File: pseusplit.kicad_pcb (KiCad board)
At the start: 2 copper layers, 231.4 x 82.6 mm, 146 parts, among them J1 USB_C_Receptacle_USB2.0_14P, J3 ST7789 320x240, Q1 DTC123J, SW1 Reset_SW, U1 IS31FL3733-QF, U2 XC6206PxxxMR, U4 STM32G0B1CBTx, U5 SRV05-4

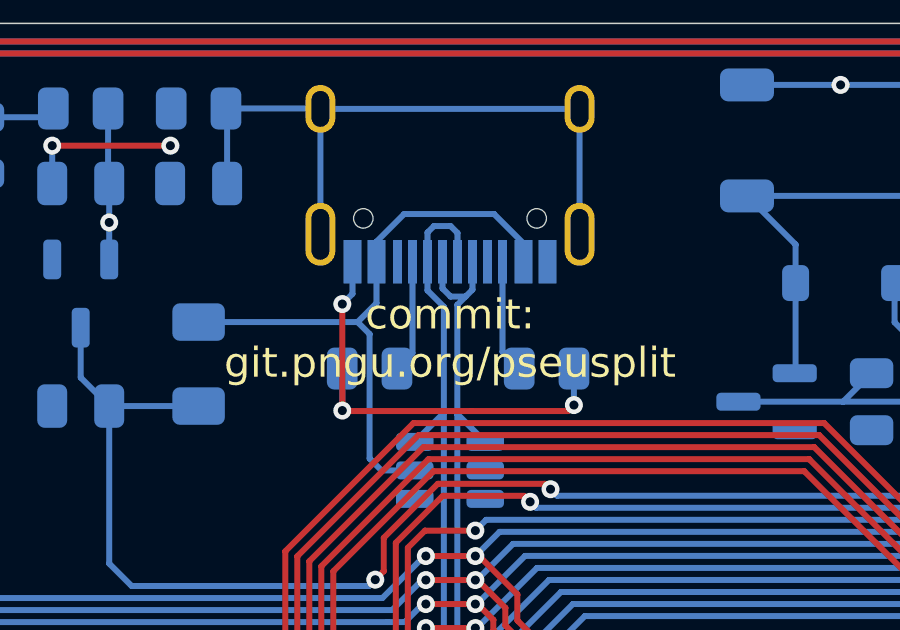
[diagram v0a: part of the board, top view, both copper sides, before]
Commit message: Add silkscreen graphics and SVG images
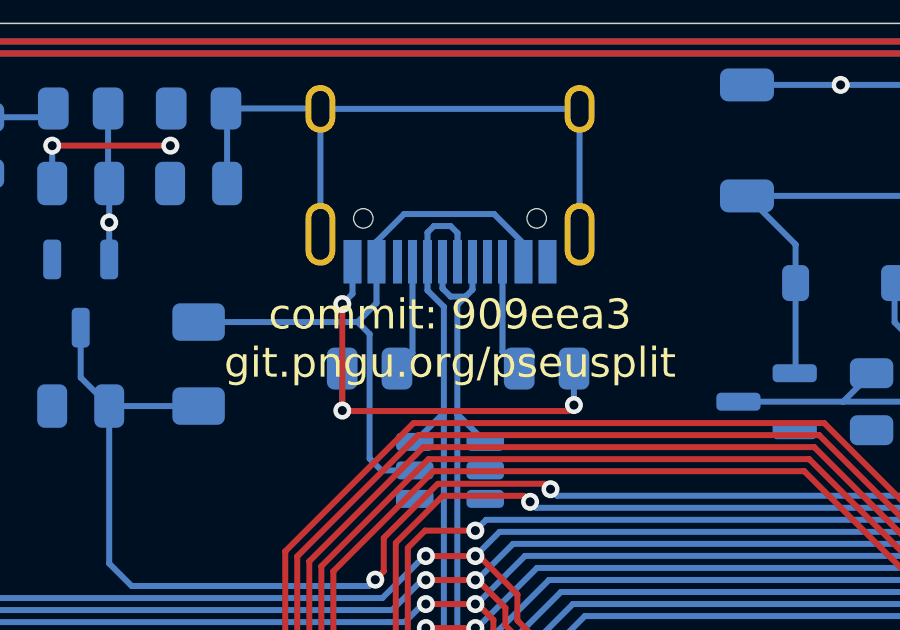
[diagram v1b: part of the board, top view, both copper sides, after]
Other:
- board text added: "commit: 909eea3 git.pngu.org/pseusplit"
- board text removed: "commit: git.pngu.org/pseusplit"
